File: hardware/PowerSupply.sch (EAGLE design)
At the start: 4 parts, among them T1 BDW73

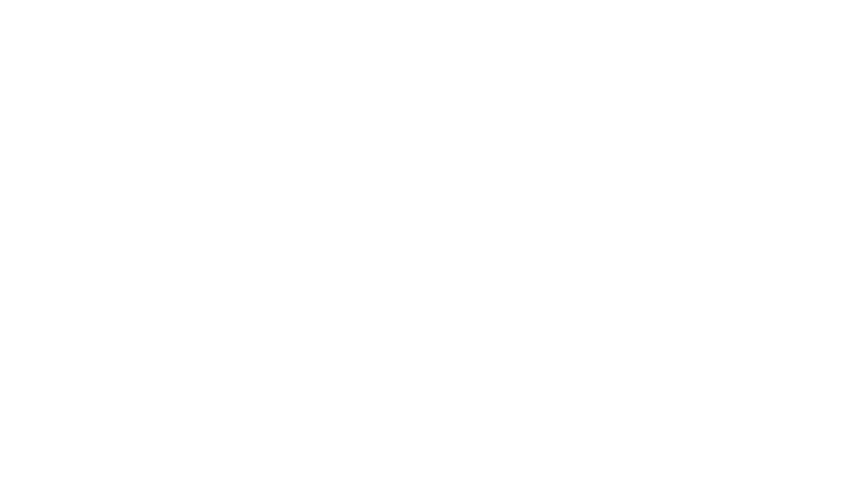
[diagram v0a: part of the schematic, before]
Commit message: added psu.lbr for unknown parts
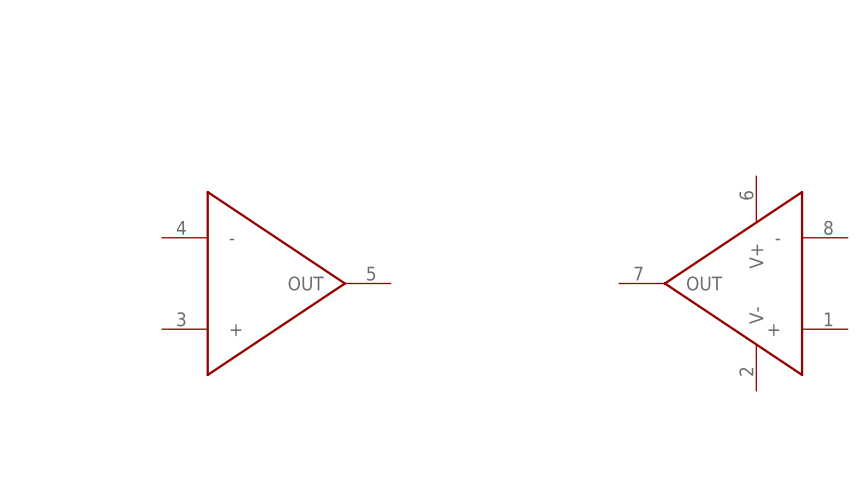
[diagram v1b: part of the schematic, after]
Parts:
- added U$1: LT1013DS8, psu:LT1013DS8
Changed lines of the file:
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@@
 <layer number="48" name="Document" color="7" fill="1" visible="no" active="no"/>
 <layer number="49" name="Reference" color="7" fill="1" visible="no" active="no"/>
+<layer number="50" name="dxf" color="7" fill="1" visible="no" active="no"/>
 <layer number="51" name="tDocu" color="7" fill="1" visible="no" active="no"/>
 <layer number="52" name="bDocu" color="7" fill="1" visible="no" active="no"/>
+<layer number="53" name="tGND_GNDA" color="7" fill="1" visible="no" active="no"/>
+<layer number="54" name="bGND_GNDA" color="7" fill="1" visible="no" active="no"/>
 <layer number="91" name="Nets" color="2" fill="1" visible="yes" active="yes"/>
 <layer number="92" name="Busses" color="1" fill="1" visible="yes" active="yes"/>
@@
 <layer number="97" name="Info" color="7" fill="1" visible="yes" active="yes"/>
 <layer number="98" name="Guide" color="6" fill="1" visible="yes" active="yes"/>
+<layer number="99" name="Anatomie" color="7" fill="1" visible="yes" active="yes"/>
+<layer number="100" name="Muster" color="7" fill="1" visible="yes" active="yes"/>
+<layer number="101" name="Patch_Top" color="7" fill="1" visible="yes" active="yes"/>
+<layer number="102" name="Brücken" color="7" fill="1" visible="yes" active="yes"/>
+<layer number="103" name="CableCode" color="7" fill="1" visible="yes" active="yes"/>
+<layer number="110" name="tdokum" color="7" fill="1" visible="yes" active="yes"/>
+<layer number="111" name="bdokum" color="7" fill="1" visible="yes" active="yes"/>
+<layer number="116" name="Patch_BOT" color="7" fill="1" visible="yes" active="yes"/>
+<layer number="125" name="_tNames" color="7" fill="1" visible="yes" active="yes"/>
+<layer number="126" name="_bNames" color="7" fill="1" visible="yes" active="yes"/>
+<layer number="199" name="L$199" color="7" fill="1" visible="yes" active="yes"/>
+<layer number="200" name="200bmp" color="7" fill="1" visible="yes" active="yes"/>
+<layer number="201" name="201bmp" color="7" fill="1" visible="yes" active="yes"/>
+<layer number="202" name="202bmp" color="7" fill="1" visible="yes" active="yes"/>
+<layer number="250" name="Descript" color="7" fill="1" visible="yes" active="yes"/>
+<layer number="251" name="SMDround" color="7" fill="1" visible="yes" active="yes"/>
+<layer number="254" name="Cool" color="7" fill="1" visible="yes" active="yes"/>
 </layers>
 <schematic xreflabel="%F%N/%S.%C%R" xrefpart="/%S.%C%R">
@@
 <part name="T1" library="transistor" deviceset="BDW73" device=""/>
 <part name="T2" library="transistor-neu-to92" deviceset="*-NPN-" device="TO92-EBC" technology="2N3904"/>
+<part name="U$1" library="psu" deviceset="LT1013DS8" device=""/>
 </parts>
 <sheets>
@@
 <instance part="T1" gate="G$1" x="76.2" y="83.82"/>
 <instance part="T2" gate="G$1" x="60.96" y="63.5"/>
+<instance part="U$1" gate="G$1" x="200.66" y="76.2" rot="MR0"/>
+<instance part="U$1" gate="G$2" x="144.78" y="76.2"/>
 </instances>
 <busses>
